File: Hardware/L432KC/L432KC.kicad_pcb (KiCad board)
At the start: 2 copper layers, 74.9 x 55.9 mm, 47 parts, among them J1 L4_G4, J2 USB_B_Micro, J3 JTAG, J4 3v3, J5 GND, J6 Conn_01x09, J7 Conn_01x08, J8 TVCC, J9 LogicAna, U1 TXS0108EPW, U2 AD8531ARTZ, U3 NUCLEO-L432KC, U4 SRV05-4, U5 SRV05-4, U6 SRV05-4

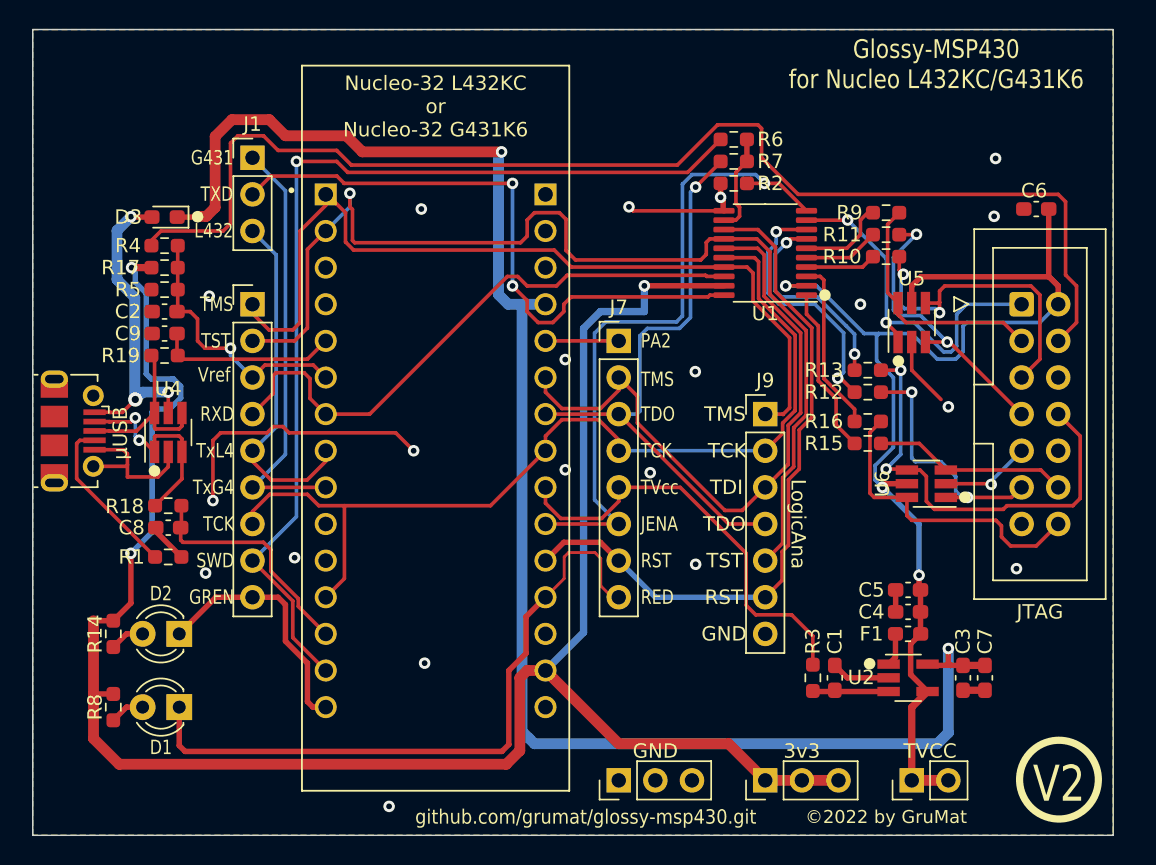
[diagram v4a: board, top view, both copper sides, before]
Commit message: Review of ESD protection for Development boards.
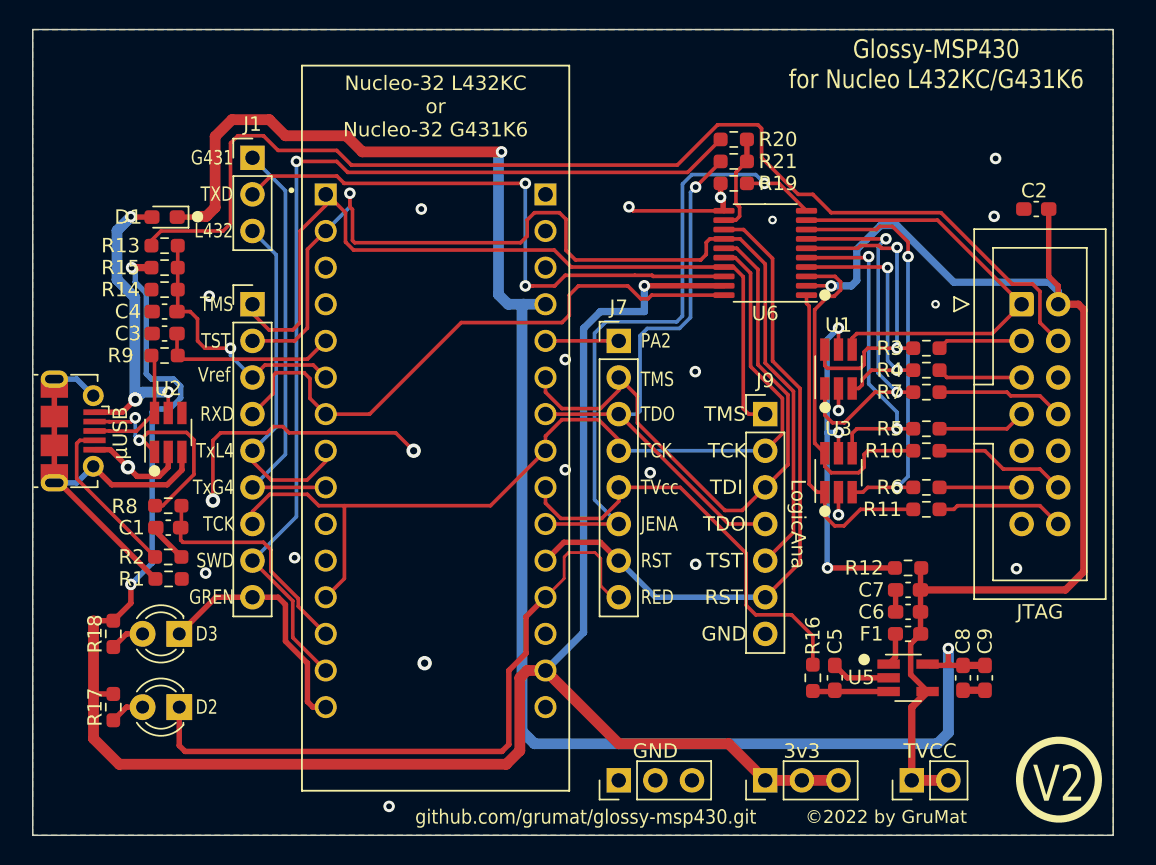
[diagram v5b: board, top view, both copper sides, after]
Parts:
- added R1: 33K, Resistor_SMD:R_0603_1608Metric_Pad0.98x0.95mm_HandSolder, F.Cu at (111.0, 113.0)
- added R12: 10K, Resistor_SMD:R_0603_1608Metric_Pad0.98x0.95mm_HandSolder, F.Cu at (162.3, 112.3)
- moved R5 13.7 mm to (163.6, 102.6)
- moved R3 9.80 mm to (163.6, 97.0)
- moved R4 8.36 mm to (163.6, 98.6)
- moved R6 7.75 mm to (163.6, 106.7)
- moved R11 7.33 mm to (163.6, 108.2)
- moved U3 6.14 mm to (157.5, 105.7), turned to 90 degrees
- moved U1 6.02 mm to (157.5, 98.5)
- moved R7 4.34 mm to (163.6, 100.1)
- moved R10 4.10 mm to (163.6, 104.1)
- renumbered C8 to C1, C6 to C2, C9 to C3, C2 to C4, C1 to C5, C4 to C6, C5 to C7, C3 to C8, C7 to C9, D3 to D1, D1 to D2, D2 to D3, R15 to R10, R16 to R11, R4 to R13, R5 to R14, R17 to R15, R3 to R16, R8 to R17, R14 to R18, R2 to R19, R1 to R2, R6 to R20, R7 to R21, R9 to R3, R10 to R4, R11 to R5, R12 to R6, R13 to R7, R18 to R8, R19 to R9, U5 to U1, U4 to U2, U6 to U3, U3 to U4, U2 to U5, U1 to U6
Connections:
- J2 pad 6: GND -> /SHIELD
- U1 pad 1: /JTDO -> /LTEST
- U1 pad 3: /JTCK -> /LTMS
- U1 pad 4: /JTMS -> /JTDO
- U1 pad 5: /TVCC -> Net-(R12-Pad2)
- U1 pad 6: /JTDI -> /LTDI
- U2 pad 3: /DM -> /SHIELD
- U2 pad 4: /DP -> unconnected-(U2-Pad4)
- U3 pad 1: /JRST -> /LRXD
- U3 pad 3: /JTXD -> /LRST
- U3 pad 4: /JTEST -> /LTCK
- U3 pad 5: /TVCC -> Net-(R12-Pad2)
- U3 pad 6: /JRXD -> /LTXD
- U6 pad 1: /LTXD -> /LRXD
- U6 pad 18: /mRXD -> /mTXD
- U6 pad 20: /mTXD -> /mRXD
- U6 pad 3: /LRXD -> /LTXD
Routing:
- net /SHIELD: track 0.00 -> 31.7 mm
- net Net-(R12-Pad2): track 0.00 -> 25.4 mm, vias 0 -> 3
- net /JTEST: track 31.1 -> 8.86 mm, vias 2 -> 0
- net /LTCK: track 5.27 -> 22.8 mm, vias 0 -> 2
- net /JTMS: track 22.6 -> 5.90 mm, vias 2 -> 0
- net /LTDI: track 6.22 -> 21.9 mm, vias 0 -> 2
- net /JTCK: track 20.5 -> 6.11 mm, vias 2 -> 0
- net /LTMS: track 4.91 -> 18.0 mm, vias 0 -> 2
- net /JRXD: track 21.7 -> 8.86 mm
- net /LTXD: track 11.7 -> 24.1 mm
- net /JRST: track 17.9 -> 5.69 mm, vias 2 -> 0
- net /LTEST: track 14.4 -> 26.0 mm
- net GND: track 59.5 -> 48.1 mm, vias 21 -> 23
- net /LRST: track 17.9 -> 29.3 mm
- net /JTDI: track 17.0 -> 5.90 mm
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
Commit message: Changed TXS0108 for TXB0304. for lower impedance. Using ESD protection of those parts.
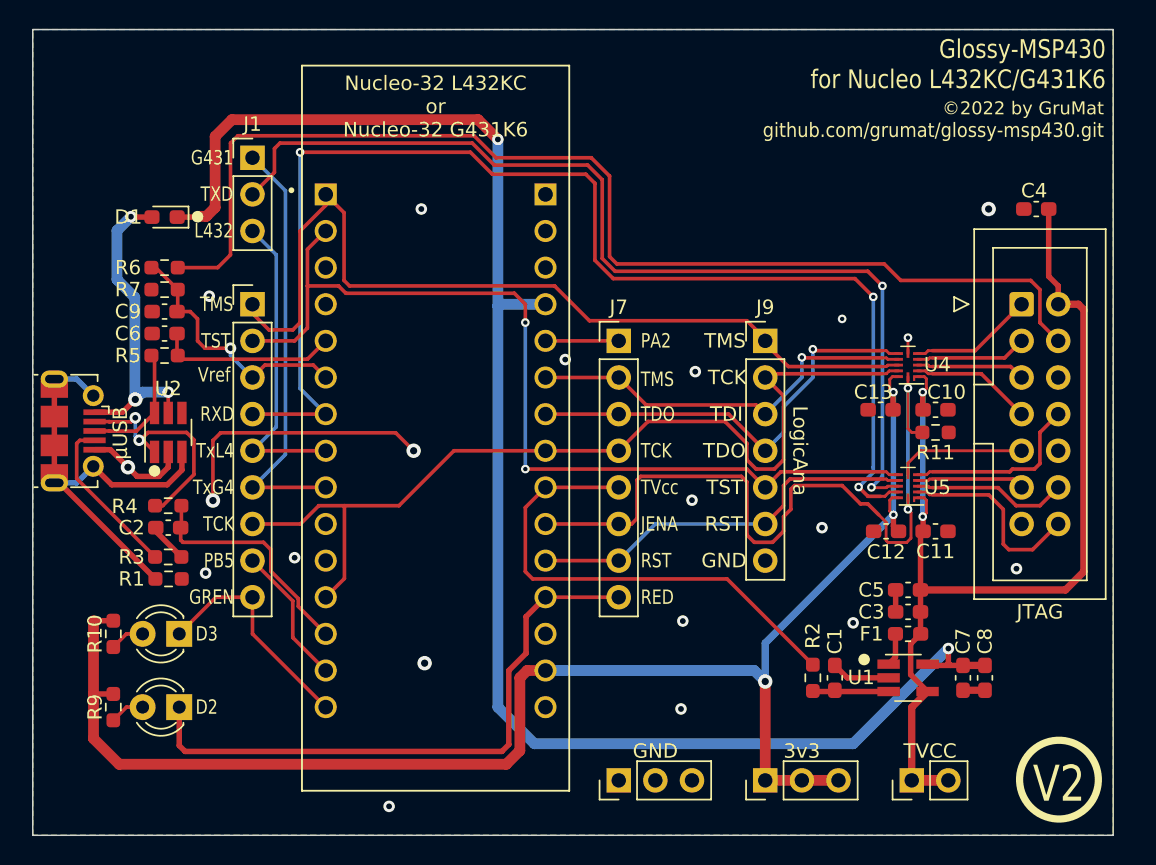
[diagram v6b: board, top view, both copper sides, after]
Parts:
- removed the R10 at (163.6, 104.1)
- removed the R11 at (163.6, 108.2)
- removed R12: 10K, Resistor_SMD:R_0603_1608Metric_Pad0.98x0.95mm_HandSolder
- removed R15: 470K, Resistor_SMD:R_0603_1608Metric_Pad0.98x0.95mm_HandSolder
- removed R20: 330, Resistor_SMD:R_0603_1608Metric_Pad0.98x0.95mm_HandSolder
- removed R21: 22, Resistor_SMD:R_0603_1608Metric_Pad0.98x0.95mm_HandSolder
- removed the R3 at (163.6, 97.0)
- removed the R4 at (163.6, 98.6)
- removed the R5 at (163.6, 102.6)
- removed the R6 at (163.6, 106.7)
- removed the R7 at (163.6, 100.1)
- removed the U1 at (157.5, 98.5)
- removed the U3 at (157.5, 105.7)
- added C10: 100nF, Capacitor_SMD:C_0603_1608Metric_Pad1.08x0.95mm_HandSolder, F.Cu at (164.2, 101.3)
- added C11: 100nF, Capacitor_SMD:C_0603_1608Metric_Pad1.08x0.95mm_HandSolder, F.Cu at (164.2, 109.7)
- added C12: 100nF, Capacitor_SMD:C_0603_1608Metric_Pad1.08x0.95mm_HandSolder, F.Cu at (160.8, 109.7)
- added C13: 100nF, Capacitor_SMD:C_0603_1608Metric_Pad1.08x0.95mm_HandSolder, F.Cu at (160.4, 101.3)
- added U4: TXB0304RUT, Package_DFN_QFN:Texas_R_PUQFN-N12, F.Cu at (162.3, 98.2)
- C2: renamed from C1; value 33p -> 22p
- C6: renamed from C3; value 33p -> 22p
- U5: renamed from U6; value TXS0108EPW -> TXB0304RUT; footprint Package_SO:TSSOP-20_4.4x6.5mm_P0.65mm -> Package_DFN_QFN:Texas_R_PUQFN-N12
- moved R11 22.2 mm to (164.2, 102.9), turned to 180 degrees
- moved U5 19.0 mm to (162.3, 106.6)
- moved J9 5.08 mm to (152.4, 96.5)
- moved R6 1.52 mm to (110.7, 91.4), turned to 0 degrees
- renumbered C5 to C1, C6 to C3, C2 to C4, C7 to C5, C8 to C7, C9 to C8, C4 to C9, R18 to R10, R19 to R11, R16 to R2, R2 to R3, R8 to R4, R9 to R5, R13 to R6, R14 to R7, R17 to R9, U5 to U1, U4 to U3
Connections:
- net /SWDO renamed /PB5
- U5 pad 1: /LRXD -> /TVCC
- U5 pad 10: /JENA -> /mRXD
- U5 pad 11: GND -> +3.3V
- U5 pad 12: Net-(R20-Pad1) -> /JENA
- U5 pad 2: /TVCC -> /JRXD
- U5 pad 3: /LTXD -> /JTXD
- U5 pad 4: /LTMS -> /JRST
- U5 pad 5: /LTCK -> /JTEST
- U5 pad 6: /LTDI -> GND
- U5 pad 7: /LTEST -> /mTEST
- U5 pad 8: /LRST -> /mRST
- U5 pad 9: /JTDO -> /mTXD
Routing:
- net /PB5: track 69.4 -> 9.72 mm, vias 1 -> 0
- net /mRXD: track 41.6 -> 87.8 mm, vias 0 -> 3
- net +3.3V: track 139.6 -> 105.9 mm
- net /LRST: track 29.3 -> 0.00 mm, vias 2 -> 0
- net /mTXD: track 40.9 -> 69.6 mm
- net /LTEST: track 26.0 -> 0.00 mm, vias 2 -> 0
- net Net-(R12-Pad2): track 25.4 -> 0.00 mm, vias 3 -> 0
- net /LTXD: track 24.1 -> 0.00 mm
- net /LRXD: track 23.0 -> 0.00 mm
- net /LTCK: track 22.8 -> 0.00 mm, vias 2 -> 0
- net /JTDO: track 30.8 -> 8.65 mm
- net /LTDI: track 21.9 -> 0.00 mm, vias 2 -> 0
- net /mRST: track 46.8 -> 27.7 mm
- net /LTMS: track 18.0 -> 0.00 mm, vias 2 -> 0
- net /mTDI: track 43.3 -> 28.0 mm, vias 0 -> 1
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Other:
- board text added: "PB5"
- board text removed: "SWD"

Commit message: Updated L432KC/G431K6 prototype board.
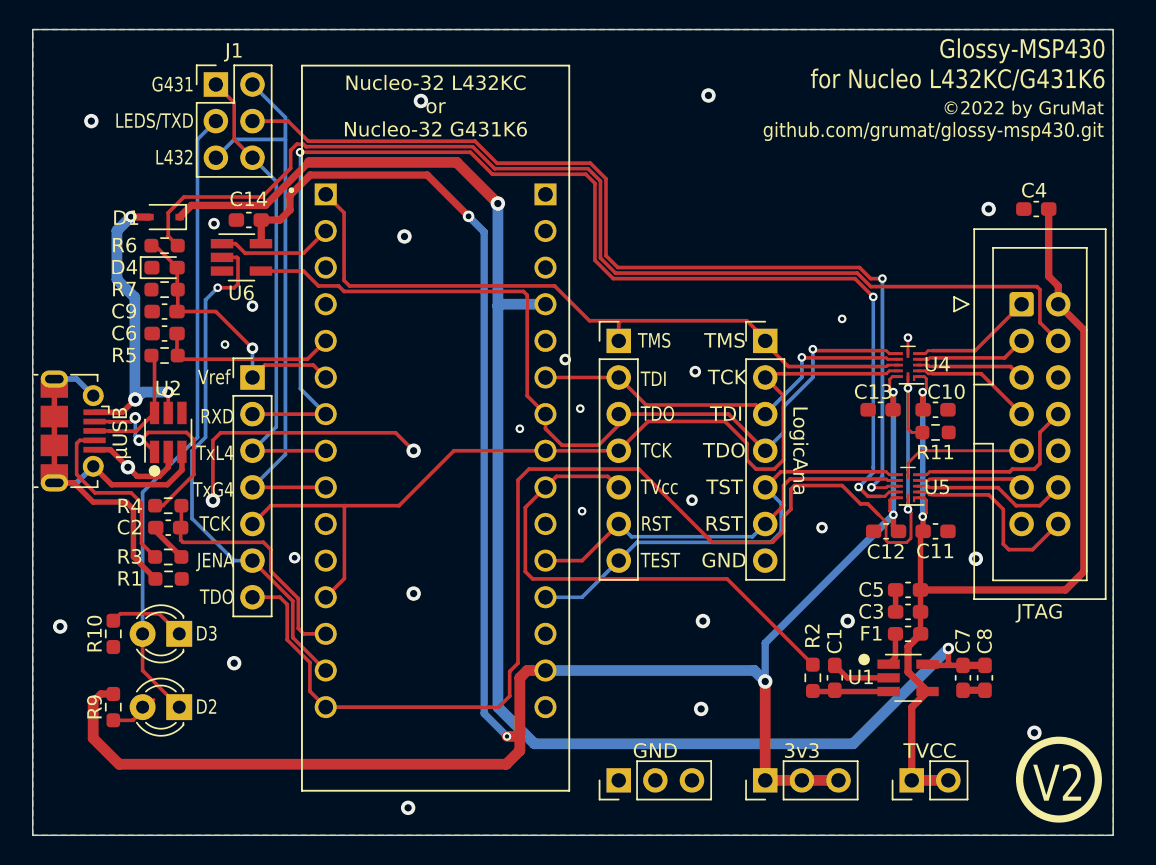
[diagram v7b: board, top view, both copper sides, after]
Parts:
- added C14: 100nF, Capacitor_SMD:C_0603_1608Metric_Pad1.08x0.95mm_HandSolder, F.Cu at (116.6, 88.1)
- added D4: 82356050050, Diode_SMD:D_0603_1608Metric_Pad1.05x0.95mm_HandSolder, F.Cu at (110.7, 91.4)
- added U6: 74LVC1G125, Package_TO_SOT_SMD:SOT-23-5_HandSoldering, F.Cu at (116.1, 90.7)
- D1: value NSR20F30NXT5G -> PMEG4010BEA,115; footprint Diode_SMD:D_0603_1608Metric_Pad1.05x0.95mm_HandSolder -> Diode_SMD:D_SOD-323
- J1: footprint Connector_PinHeader_2.54mm:PinHeader_1x03_P2.54mm_Vertical -> Connector_PinHeader_2.54mm:PinHeader_2x03_P2.54mm_Vertical
- J6: value Conn_01x09 -> Conn_01x07; footprint Connector_PinHeader_2.54mm:PinHeader_1x09_P2.54mm_Vertical -> Connector_PinHeader_2.54mm:PinHeader_1x07_P2.54mm_Vertical
- J7: value Conn_01x08 -> Conn_01x07_Male; footprint Connector_PinHeader_2.54mm:PinHeader_1x08_P2.54mm_Vertical -> Connector_PinHeader_2.54mm:PinHeader_1x07_P2.54mm_Vertical
- moved J1 5.68 mm to (114.3, 78.7)
- moved J6 5.08 mm to (116.8, 99.1)
- moved R6 1.52 mm to (110.7, 89.9)
- turned R10 to -90 degrees
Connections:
- net /TVCC renamed VDC
- D2 pad 1: /LED_RED -> /LEDS
- D3 pad 1: /LED_GR -> Net-(R10-Pad1)
- D3 pad 2: Net-(D3-Pad2) -> /LEDS
- J1 pad 1: /TXD_G4 -> /TXD_L4
- J1 pad 2: /mTXD -> /TXD_G4
- J1 pad 3: /TXD_L4 -> /LEDS
- J6 pad 1: /mTMS -> /VREF_2
- J6 pad 2: /mTEST -> /mRXD
- J6 pad 3: /VREF_2 -> /TXD_L4
- J6 pad 4: /mRXD -> /TXD_G4
- J6 pad 5: /TXD_L4 -> /mTCK
- J6 pad 6: /TXD_G4 -> /SBW_OUT
- J6 pad 7: /mTCK -> /JENA
- J7 pad 1: /PA2 -> /mTMS
- J7 pad 6: /JENA -> /mRST
- J7 pad 7: /mRST -> /mTEST
- R10 pad 1: Net-(D3-Pad2) -> Net-(R10-Pad1)
- R10 pad 2: +3.3V -> GND
- U3 pad CN3_14: /PB5 -> /SBW_OUT
- U3 pad CN3_15: /LED_GR -> /JENA
- U3 pad CN3_2: /mTEST -> /SBW_DIR
- U3 pad CN4_10: /JENA -> unconnected-(U3-PadCN4_10)
- U3 pad CN4_12: /LED_RED -> /mTEST
- U3 pad CN4_5: /PA2 -> unconnected-(U3-PadCN4_5)
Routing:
- net +3.3V: track 105.9 -> 156.3 mm, vias 3 -> 5
- net /LEDS: track 0.00 -> 43.8 mm
- net /LED_RED: track 42.2 -> 0.00 mm
- net /JENA: track 53.9 -> 90.4 mm
- net /SBW_OUT: track 0.00 -> 36.3 mm, vias 0 -> 1
- net /mTEST: track 65.4 -> 31.5 mm, vias 2 -> 0
- net /mTDO: track 30.8 -> 61.5 mm
- net /LED_GR: track 15.9 -> 0.00 mm
- net /mTMS: track 61.9 -> 49.1 mm
- net /TXD_L4: track 21.7 -> 32.9 mm
- net /TXD_G4: track 29.8 -> 40.3 mm
- net /PB5: track 9.72 -> 0.00 mm
- net +5V: track 111.5 -> 103.4 mm
- net /SBW_DIR: track 0.00 -> 8.10 mm
- net Net-(R10-Pad1): track 0.00 -> 5.35 mm
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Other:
- board text added: "LEDS/TXD"
- board text added: "TEST"
- board text removed: "GREN"
- board text removed: "PA2"
- board text removed: "PB5"
- board text removed: "RED"
- board text removed: "TXD"
